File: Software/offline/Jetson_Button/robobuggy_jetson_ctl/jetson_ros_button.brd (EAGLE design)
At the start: 100 x 80 mm, 4 parts, among them J1 22-27-2061-06

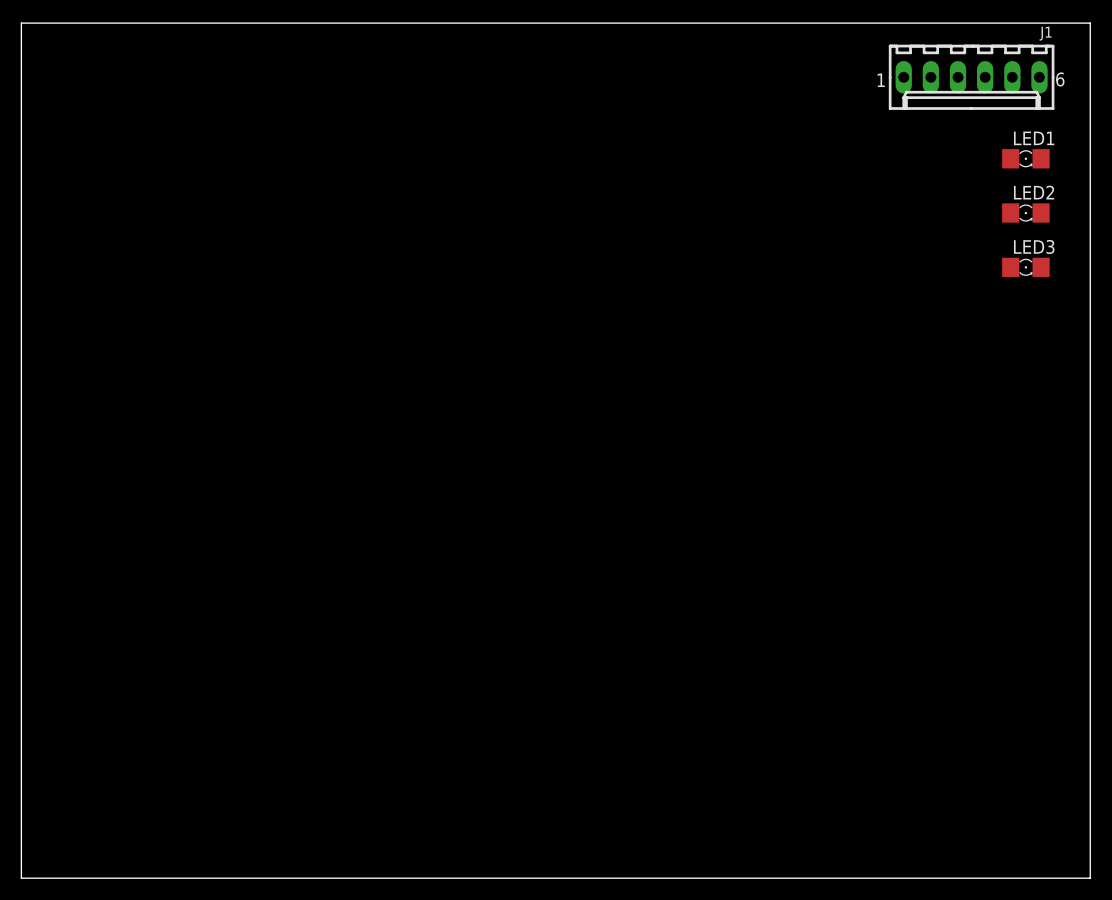
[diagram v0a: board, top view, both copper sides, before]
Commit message: Added in resistors and arranged PCB layout
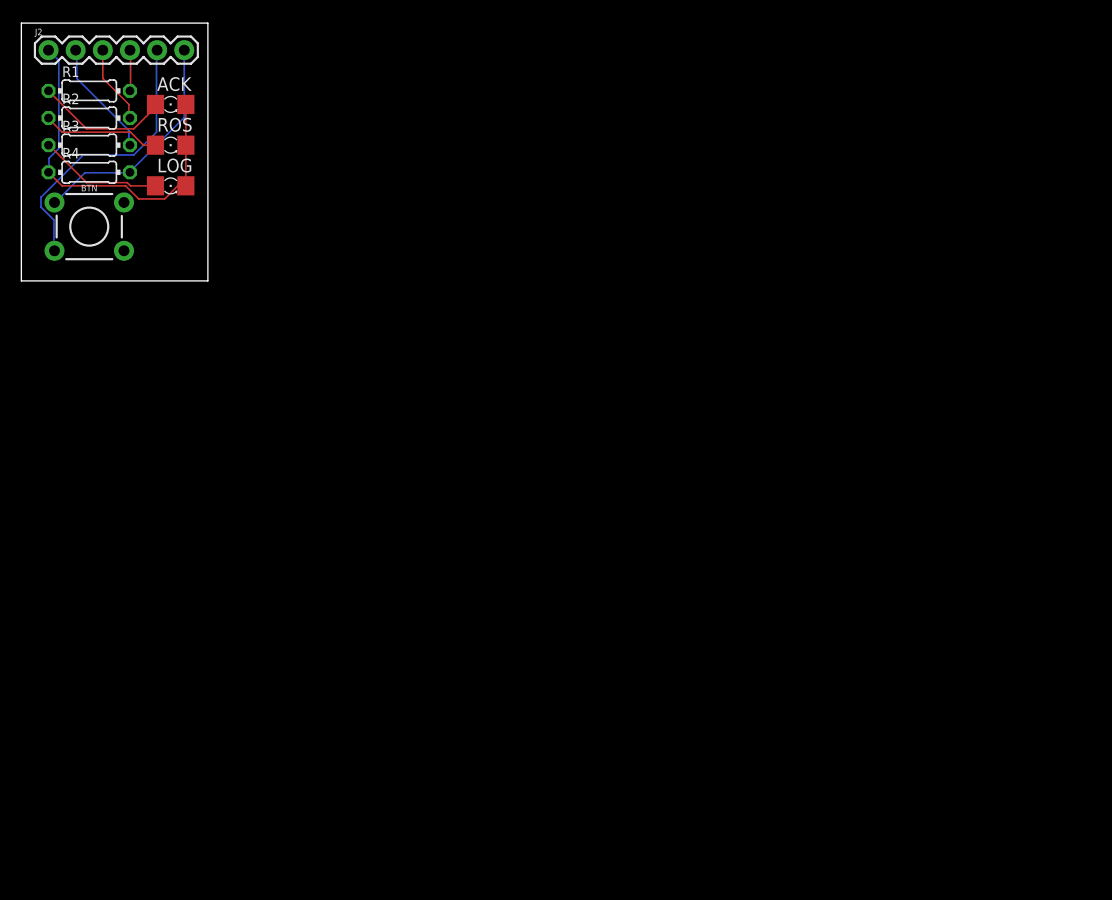
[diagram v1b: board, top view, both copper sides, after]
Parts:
- removed J1: 22-27-2061-06, con-molex:6410-06
- removed LED1, LED2, LED3: (no value), eagle-ltspice:LED_1206
- added ACK, LOG, ROS: (no value), eagle-ltspice:LED_1206
- added BTN: START_LOG, SparkFun-Switches:TACTILE_SWITCH_PTH_6.0MM
- added J2: (no value), SparkFun-Connectors:1X06
- added R1, R2, R3, R4: (no value), rcl:0204/7
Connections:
- new net N$1: ACK.A, R1.1
- new net N$2: R2.1, ROS.A
- new net N$3: LOG.A, R3.1
- net 3.3V: now also BTN.1, J2.6, R4.2; no longer J1.1
- net ACK: now also J2.4, R1.2; no longer J1.3
- net BTN: now also BTN.3, J2.5; no longer J1.2
- net GND: now also ACK.C, J2.1, LOG.C, R4.1, ROS.C; no longer J1.6, LED1.C, LED2.C, LED3.C
- net LOG: now also J2.2, R3.2; no longer J1.5
- net ROS: now also J2.3, R2.2; no longer J1.4
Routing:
- net GND: track 0.00 -> 34.2 mm
- net BTN: track 0.00 -> 26.6 mm
- net 3.3V: track 0.00 -> 21.7 mm
- net N$1: track 0.00 -> 12.6 mm
- net N$3: track 0.00 -> 11.6 mm
- net N$2: track 0.00 -> 11.1 mm
- net LOG: track 0.00 -> 11.1 mm
- net ROS: track 0.00 -> 7.42 mm
- net ACK: track 0.00 -> 3.84 mm
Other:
- board size 100 x 80 mm -> 17.4 x 24.1 mm
- board text added: "Robobuggy Jetson Ext. Ctl. Rev 1.0"
